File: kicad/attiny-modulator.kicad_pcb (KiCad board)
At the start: 2 copper layers, 0 parts

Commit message: Updating schematic, layout and front panel
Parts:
- added C1: 100nF, Rumblesan_Standard_Parts:C_Rect_L7.0mm_W2.5mm_P5.00mm, F.Cu at (153.2, 66.5)
- added C10: 100nF, Rumblesan_Standard_Parts:C_Rect_L7.0mm_W2.5mm_P5.00mm, F.Cu at (138.5, 110.0)
- added C12: 1nF, Rumblesan_Standard_Parts:C_Rect_L7.0mm_W2.5mm_P5.00mm, F.Cu at (145.8, 78.8)
- added C2: 100nF, Rumblesan_Standard_Parts:C_Rect_L7.0mm_W2.5mm_P5.00mm, F.Cu at (157.5, 63.0)
- added C3: 10uF, Rumblesan_Standard_Parts:CP_Radial_D5.0mm_P2.00mm, F.Cu at (144.3, 60.2)
- added C4: 1nF, Rumblesan_Standard_Parts:C_Rect_L7.0mm_W2.5mm_P5.00mm, F.Cu at (153.9, 100.3)
- added C5: 10uF, Rumblesan_Standard_Parts:CP_Radial_D5.0mm_P2.00mm, F.Cu at (150.9, 60.2)
- added C6: 100nF, Rumblesan_Standard_Parts:C_Rect_L7.0mm_W2.5mm_P5.00mm, F.Cu at (145.8, 89.4)
- added C7: 100nF, Rumblesan_Standard_Parts:C_Rect_L7.0mm_W2.5mm_P5.00mm, F.Cu at (156.7, 140.5)
- added C8: 100nF, Rumblesan_Standard_Parts:C_Rect_L7.0mm_W2.5mm_P5.00mm, F.Cu at (141.0, 137.8)
- added C9: 1n8F, Rumblesan_Standard_Parts:C_Rect_L7.0mm_W3.5mm_P5.00mm, F.Cu at (146.3, 125.0)
- added D1: 1N5158, Rumblesan_Standard_Parts:D_DO-41_SOD81_P10.16mm_Horizontal, F.Cu at (149.6, 55.6)
- added D2: 1N5158, Rumblesan_Standard_Parts:D_DO-41_SOD81_P10.16mm_Horizontal, F.Cu at (139.4, 52.3)
- added D3: LED, LED_THT:LED_D1.8mm_W3.3mm_H2.4mm, B.Cu at (115.8, 137.5)
- added D4: LED, LED_THT:LED_D1.8mm_W3.3mm_H2.4mm, B.Cu at (113.2, 141.0)
- added D5: LED, LED_THT:LED_D1.8mm_W3.3mm_H2.4mm, B.Cu at (105.2, 104.5)
- added D6: 1N4148, Rumblesan_Standard_Parts:D_DO-35_SOD27_P7.62mm_Horizontal, F.Cu at (116.0, 109.6)
- added H1: MountingHole_Pad, MountingHole:MountingHole_3.2mm_M3_DIN965_Pad, F.Cu at (103.5, 136.5)
- added H2: MountingHole_Pad, MountingHole:MountingHole_3.2mm_M3_DIN965_Pad, F.Cu at (103.5, 53.5)
- added H3: MountingHole_Pad, MountingHole:MountingHole_3.2mm_M3_DIN965_Pad, F.Cu at (134.5, 136.5)
- added H4: MountingHole_Pad, MountingHole:MountingHole_3.2mm_M3_DIN965_Pad, F.Cu at (134.5, 53.5)
- added J1: Eurorack Power Small, Eurorack_Power:Eurorack_PowerHeader_2x05_P2.54mm_Shrouded, F.Cu at (135.0, 64.5)
- added J10: Conn_01x04_Socket, Connector_PinSocket_2.54mm:PinSocket_1x04_P2.54mm_Vertical, F.Cu at (119.0, 71.0)
- added J11: Eurorack Mono Jack, Rumblesan_Standard_Parts:Jack_3.5mm_QingPu_WQP-PJ398SM_Vertical, B.Cu at (122.5, 149.5)
- added J12: Conn_01x05_Pin, Connector_PinHeader_2.54mm:PinHeader_1x05_P2.54mm_Vertical, B.Cu at (145.5, 145.5)
- added J13: Conn_01x05_Socket, Connector_PinSocket_2.54mm:PinSocket_1x05_P2.54mm_Vertical, F.Cu at (114.5, 145.5)
- added J2: Eurorack Mono Jack, Rumblesan_Standard_Parts:Jack_3.5mm_QingPu_WQP-PJ398SM_Vertical, B.Cu at (106.5, 123.5)
- added J3: Eurorack Mono Jack, Rumblesan_Standard_Parts:Jack_3.5mm_QingPu_WQP-PJ398SM_Vertical, B.Cu at (122.5, 104.5)
- added J4: Eurorack Mono Jack, Rumblesan_Standard_Parts:Jack_3.5mm_QingPu_WQP-PJ398SM_Vertical, B.Cu at (106.5, 149.5)
- added J5: Eurorack Mono Jack, Rumblesan_Standard_Parts:Jack_3.5mm_QingPu_WQP-PJ398SM_Vertical, B.Cu at (122.5, 123.5)
- added J6: AVR-ISP-6, Connector_PinHeader_2.54mm:PinHeader_2x03_P2.54mm_Vertical, F.Cu at (136.9, 116.3)
- added J7: Conn_01x04_Socket, Connector_PinSocket_2.54mm:PinSocket_1x04_P2.54mm_Vertical, F.Cu at (109.0, 83.0)
- added J8: Conn_01x04_Pin, Connector_PinHeader_2.54mm:PinHeader_1x04_P2.54mm_Vertical, B.Cu at (140.0, 83.0)
- added J9: Conn_01x04_Pin, Connector_PinHeader_2.54mm:PinHeader_1x04_P2.54mm_Vertical, B.Cu at (150.0, 71.0)
- added JP2: Jumper_2_Open, Connector_PinHeader_2.54mm:PinHeader_1x02_P2.54mm_Vertical, F.Cu at (153.2, 114.3)
- added JP3: Jumper_2_Open, Connector_PinHeader_2.54mm:PinHeader_1x02_P2.54mm_Vertical, F.Cu at (149.4, 116.8)
- added Q1: BC547, Package_TO_SOT_THT:TO-92_Inline_Wide, F.Cu at (102.6, 112.3)
- added Q2: BC547, Package_TO_SOT_THT:TO-92_Inline_Wide, F.Cu at (106.6, 95.0)
- added Q3: BC547, Package_TO_SOT_THT:TO-92_Inline_Wide, F.Cu at (111.5, 107.7)
- added R1: 200k, Rumblesan_Standard_Parts:R_Axial_DIN0207_L6.3mm_D2.5mm_P10.16mm_Horizontal, F.Cu at (151.9, 145.0)
- added R10: 100k, Rumblesan_Standard_Parts:R_Axial_DIN0207_L6.3mm_D2.5mm_P10.16mm_Horizontal, F.Cu at (150.9, 110.2)
- added R11: 100k, Rumblesan_Standard_Parts:R_Axial_DIN0207_L6.3mm_D2.5mm_P10.16mm_Horizontal, F.Cu at (142.7, 130.0)
- added R13: 10k, Rumblesan_Standard_Parts:R_Axial_DIN0207_L6.3mm_D2.5mm_P10.16mm_Horizontal, F.Cu at (152.9, 130.3)
- added R17: 1k, Rumblesan_Standard_Parts:R_Axial_DIN0207_L6.3mm_D2.5mm_P10.16mm_Horizontal, F.Cu at (126.5, 133.5)
- added R18: 100k, Rumblesan_Standard_Parts:R_Axial_DIN0207_L6.3mm_D2.5mm_P10.16mm_Horizontal, F.Cu at (116.3, 113.5)
- added R19: 10k, Rumblesan_Standard_Parts:R_Axial_DIN0207_L6.3mm_D2.5mm_P10.16mm_Horizontal, F.Cu at (113.5, 117.0)
- added R2: 200k, Rumblesan_Standard_Parts:R_Axial_DIN0207_L6.3mm_D2.5mm_P10.16mm_Horizontal, F.Cu at (136.4, 95.2)
- added R20: 100k, Rumblesan_Standard_Parts:R_Axial_DIN0207_L6.3mm_D2.5mm_P10.16mm_Horizontal, F.Cu at (102.0, 97.8)
- added R21: 47k, Rumblesan_Standard_Parts:R_Axial_DIN0207_L6.3mm_D2.5mm_P10.16mm_Horizontal, F.Cu at (105.4, 80.0)
- added R22: 100k, Rumblesan_Standard_Parts:R_Axial_DIN0207_L6.3mm_D2.5mm_P10.16mm_Horizontal, F.Cu at (111.5, 104.1)
- added R23: R_led, Rumblesan_Standard_Parts:R_Axial_DIN0207_L6.3mm_D2.5mm_P10.16mm_Horizontal, F.Cu at (102.4, 90.2)
- added R24: 200k, Rumblesan_Standard_Parts:R_Axial_DIN0207_L6.3mm_D2.5mm_P10.16mm_Horizontal, F.Cu at (158.0, 112.8)
- added R25: 200k, Rumblesan_Standard_Parts:R_Axial_DIN0207_L6.3mm_D2.5mm_P10.16mm_Horizontal, F.Cu at (154.9, 86.4)
- added R26: 100k, Rumblesan_Standard_Parts:R_Axial_DIN0207_L6.3mm_D2.5mm_P10.16mm_Horizontal, F.Cu at (151.9, 86.4)
- added R3: 200k, Rumblesan_Standard_Parts:R_Axial_DIN0207_L6.3mm_D2.5mm_P10.16mm_Horizontal, F.Cu at (148.8, 76.2)
- added R4: 200k, Rumblesan_Standard_Parts:R_Axial_DIN0207_L6.3mm_D2.5mm_P10.16mm_Horizontal, F.Cu at (158.0, 86.4)
- added R5: 100k, Rumblesan_Standard_Parts:R_Axial_DIN0207_L6.3mm_D2.5mm_P10.16mm_Horizontal, F.Cu at (157.0, 110.2)
- added R6: 1k, Rumblesan_Standard_Parts:R_Axial_DIN0207_L6.3mm_D2.5mm_P10.16mm_Horizontal, F.Cu at (141.0, 155.7)
- added R7: 100k, Rumblesan_Standard_Parts:R_Axial_DIN0207_L6.3mm_D2.5mm_P10.16mm_Horizontal, F.Cu at (147.8, 110.2)
- added R8: 100k, Rumblesan_Standard_Parts:R_Axial_DIN0207_L6.3mm_D2.5mm_P10.16mm_Horizontal, F.Cu at (139.7, 119.9)
- added R9: 100k, Rumblesan_Standard_Parts:R_Axial_DIN0207_L6.3mm_D2.5mm_P10.16mm_Horizontal, F.Cu at (149.9, 120.1)
- added RV1: 10k, Rumblesan_Standard_Parts:Potentiometer_Alpha_RD901F-40-00D_Single_Vertical, B.Cu at (122.5, 57.5)
- added RV2: 10k, Rumblesan_Standard_Parts:Potentiometer_Alpha_RD901F-40-00D_Single_Vertical, B.Cu at (106.5, 69.5)
- added RV3: 10k, Rumblesan_Standard_Parts:Potentiometer_Alpha_RD901F-40-00D_Single_Vertical, B.Cu at (122.5, 81.5)
- added U1: ATtiny85-20P, Package_DIP:DIP-8_W7.62mm, F.Cu at (144.3, 106.4)
- added U2: MCP602, Package_DIP:DIP-8_W7.62mm_Socket, F.Cu at (149.4, 97.0)
- added U4: L78L05_TO92, Package_TO_SOT_THT:TO-92_Inline_Wide, F.Cu at (145.0, 69.6)
- added U5: L79L05_TO92, Package_TO_SOT_THT:TO-92_Inline_Wide, F.Cu at (152.9, 53.8)
- added U6: TL072, Package_DIP:DIP-8_W7.62mm, F.Cu at (152.7, 132.8)
- added mouse-bite-2mm-slot: VAL**, Panelization:mouse-bite-2mm-slot, F.Cu at (130.0, 90.0)
- added mouse-bite-2mm-slot: VAL**, Panelization:mouse-bite-2mm-slot, F.Cu at (130.0, 110.0)
- added mouse-bite-2mm-slot: VAL**, Panelization:mouse-bite-2mm-slot, F.Cu at (130.0, 150.0)
- added mouse-bite-2mm-slot: VAL**, Panelization:mouse-bite-2mm-slot, F.Cu at (130.0, 130.0)
- added mouse-bite-2mm-slot: VAL**, Panelization:mouse-bite-2mm-slot, F.Cu at (130.0, 65.0)
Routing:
- net +5V: track 0.00 -> 146.7 mm
- net VCC: track 0.00 -> 112.1 mm
- net VEE: track 0.00 -> 103.0 mm
- net Net-(U2A--): track 0.00 -> 85.8 mm
- net -5V: track 0.00 -> 55.5 mm
- net /MCU_ADC_1: track 0.00 -> 52.3 mm
- net /OUT_MAIN: track 0.00 -> 52.1 mm
- net Net-(U2B--): track 0.00 -> 47.3 mm
- net /MCU_PWM: track 0.00 -> 39.3 mm
- net /CV2_MAIN: track 0.00 -> 38.0 mm
- net /CV1_CTRL: track 0.00 -> 32.4 mm
- net /MCU_ADC_2: track 0.00 -> 29.9 mm, vias 0 -> 1
- net Net-(J11-Tip): track 0.00 -> 29.4 mm
- net /CV2_CTRL: track 0.00 -> 28.0 mm
- net /POT1_CTRL: track 0.00 -> 26.7 mm
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- added copper zone on B.Cu, net GND
- added copper zone on F.Cu, net GND
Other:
- board outline added: 60 x 108 mm

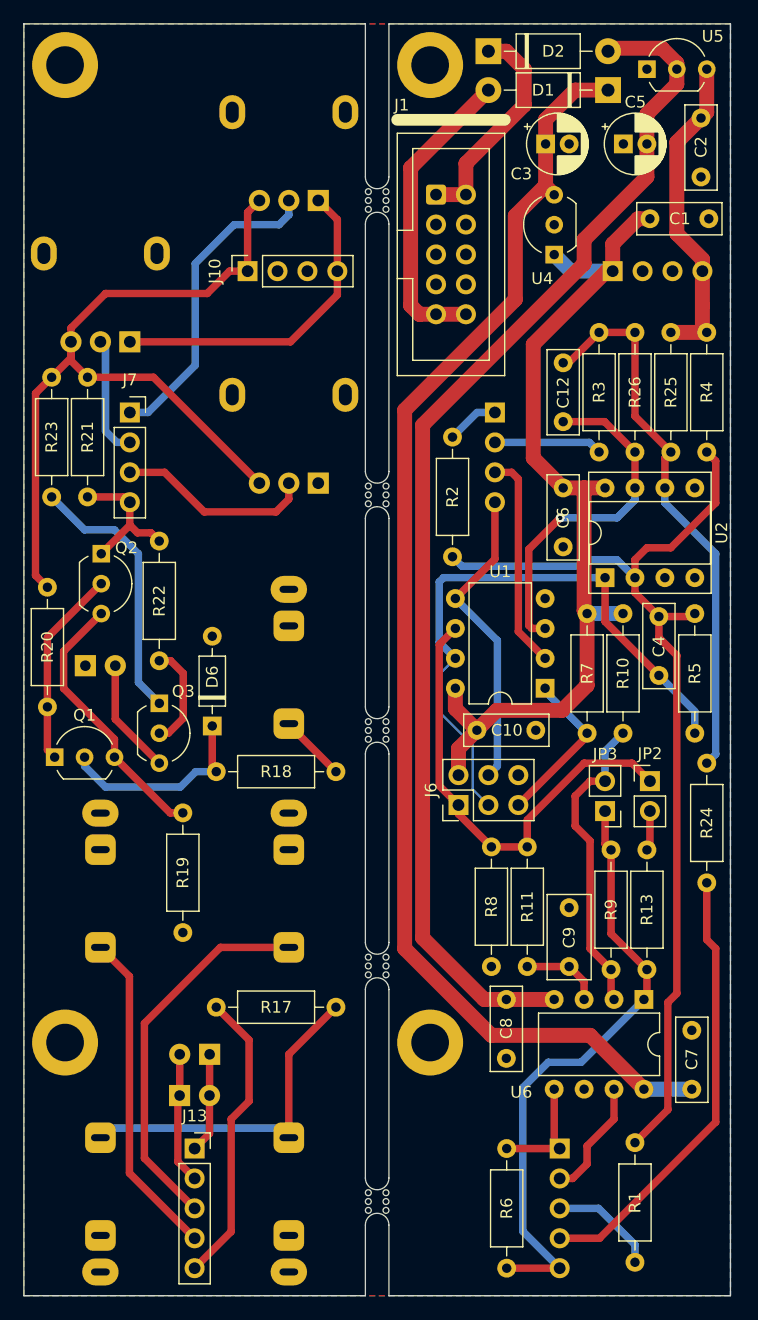
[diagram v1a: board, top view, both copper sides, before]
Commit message: Fixing bugs with circuit
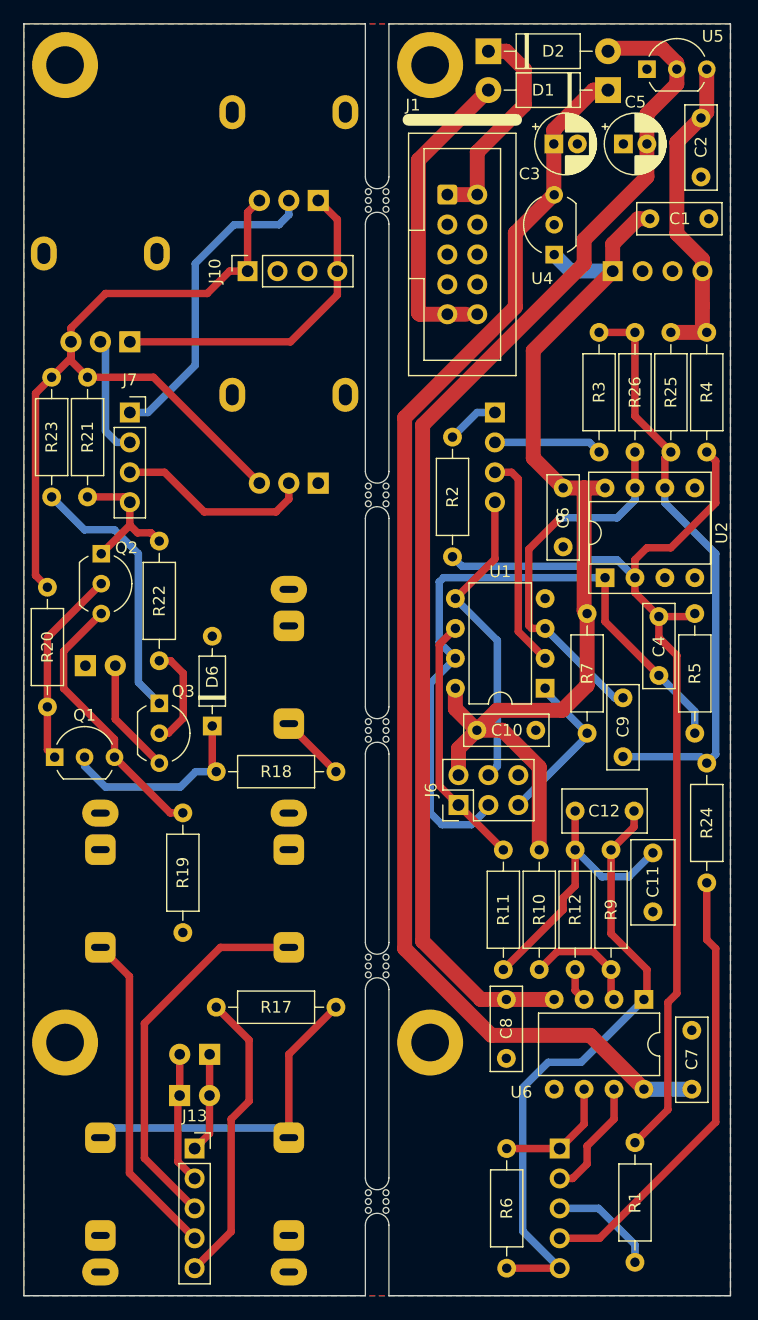
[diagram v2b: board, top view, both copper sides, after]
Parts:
- removed JP2, JP3: Jumper_2_Open, Connector_PinHeader_2.54mm:PinHeader_1x02_P2.54mm_Vertical
- removed R13: 10k, Rumblesan_Standard_Parts:R_Axial_DIN0207_L6.3mm_D2.5mm_P10.16mm_Horizontal
- removed R8: 100k, Rumblesan_Standard_Parts:R_Axial_DIN0207_L6.3mm_D2.5mm_P10.16mm_Horizontal
- added C11: 1nF, Rumblesan_Standard_Parts:C_Rect_L7.0mm_W3.5mm_P5.00mm, F.Cu at (153.4, 125.4)
- added R12: 22k, Rumblesan_Standard_Parts:R_Axial_DIN0207_L6.3mm_D2.5mm_P10.16mm_Horizontal, F.Cu at (146.8, 130.3)
- C12: value 1nF -> 2.2nF; footprint Rumblesan_Standard_Parts:C_Rect_L7.0mm_W2.5mm_P5.00mm -> Rumblesan_Standard_Parts:C_Rect_L7.0mm_W3.5mm_P5.00mm
- C9: value 1n8F -> 1nF; footprint Rumblesan_Standard_Parts:C_Rect_L7.0mm_W3.5mm_P5.00mm -> Rumblesan_Standard_Parts:C_Rect_L7.0mm_W2.5mm_P5.00mm
- R11: value 100k -> 22k
- moved C12 38.5 mm to (151.8, 116.8), turned to 180 degrees
- moved R10 21.3 mm to (143.8, 130.3)
- moved C9 13.6 mm to (150.9, 112.2), turned to 90 degrees
- moved R11 10.1 mm to (140.7, 120.1), turned to -90 degrees
- moved J1 0.96 mm to (136.0, 64.5)
- moved C3 0.70 mm to (145.0, 60.2)
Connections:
- C12 pad 1: Net-(U2B--) -> /OUT_MAIN
- C12 pad 2: /MCU_ADC_2 -> Net-(C11-Pad2)
- C9 pad 1: GND -> Net-(U2B--)
- C9 pad 2: Net-(U6A-+) -> /MCU_ADC_2
- J2 pad 3: unconnected-(J2-Tip_normalize-Pad3) -> GND
- J5 pad 3: unconnected-(J5-Tip_normalize-Pad3) -> GND
- R11 pad 1: Net-(U6A-+) -> /MCU_PWM
- R11 pad 2: /MCU_PWM -> Net-(C11-Pad2)
- U6 pad 5: /LED_NEG_MAIN -> GND
- U6 pad 6: GND -> /LED_NEG_MAIN
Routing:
- net Net-(C11-Pad2): track 0.00 -> 24.4 mm
- net /MCU_PWM: track 39.3 -> 21.6 mm
- net Net-(U6A--): track 26.4 -> 10.0 mm
- net +5V: track 146.7 -> 156.9 mm
- net /MCU_ADC_1: track 52.3 -> 57.8 mm
- net Net-(U6A-+): track 6.88 -> 2.86 mm
- net Net-(JP2-B): track 3.41 -> 0.00 mm
- net Net-(U2B--): track 47.3 -> 50.5 mm
- net VCC: track 112.1 -> 110.2 mm
- net /MCU_ADC_2: track 29.9 -> 31.8 mm
- net /LED_NEG_MAIN: track 9.73 -> 10.4 mm
- net /OUT_MAIN: track 52.1 -> 52.7 mm
- net Net-(D1-A): track 26.0 -> 25.5 mm

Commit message: Refreshing board layout
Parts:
- added REF**: BCM_Logo_tiny_Copper_8mmx8mm, BCM_Graphics:BCM_Logo_tiny_Copper_8mmx8mm, F.Cu at (135.4, 153.7)
- C11, C12: footprint Rumblesan_Standard_Parts:C_Rect_L7.0mm_W3.5mm_P5.00mm -> Rumblesan_Standard_Parts:C_Rect_L7.0mm_W2.5mm_P5.00mm
- J1: footprint Eurorack_Power:Eurorack_PowerHeader_2x05_P2.54mm_Shrouded -> Rumblesan_Eurorack_Power:Eurorack_PowerHeader_2x05_P2.54mm_Shrouded
- J11, J2, J3, J4, J5: footprint Rumblesan_Standard_Parts:Jack_3.5mm_QingPu_WQP-PJ398SM_Vertical -> Rumblesan_Audio_Connectors:Jack_3.5mm_QingPu_WQP-PJ398SM_Vertical
- RV1, RV2, RV3: footprint Rumblesan_Standard_Parts:Potentiometer_Alpha_RD901F-40-00D_Single_Vertical -> Rumblesan_Potentiometer_THT:Potentiometer_Alpha_RD901F-40-00D_Single_Vertical
- U1, U6: footprint Package_DIP:DIP-8_W7.62mm -> Package_DIP:DIP-8_W7.62mm_Socket
- mouse-bite-2mm-slot (x5): footprint Panelization:mouse-bite-2mm-slot -> Rumblesan_Panelization:mouse-bite-2mm-slot
- moved C7 0.25 mm to (156.7, 140.7)
- moved U6 0.25 mm to (152.7, 133.1)
- moved R6 0.22 mm to (141.2, 155.7)
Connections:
- R17 pad 1: Net-(J11-Tip) -> Net-(J11-PadT)
- R18 pad 2: Net-(J3-Tip) -> Net-(J3-PadT)
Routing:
- net Net-(J11-Tip): track 29.4 -> 0.00 mm
- net Net-(J11-PadT): track 0.00 -> 29.4 mm
- net Net-(J3-Tip): track 5.74 -> 0.00 mm
- net Net-(J3-PadT): track 0.00 -> 5.74 mm
- net /MCU_ADC_1: track 57.8 -> 53.6 mm
- net /MCU_ADC_2: track 31.8 -> 35.2 mm, vias 1 -> 0
- net +5V: track 156.9 -> 154.6 mm
- net /OUT_MAIN: track 52.7 -> 51.4 mm
- net /MCU_TRIG: track 26.4 -> 27.6 mm
- net /MCU_RESET: track 13.8 -> 15.0 mm
- net /LED_POS_MAIN: track 10.1 -> 9.24 mm
- net Net-(D2-K): track 18.5 -> 17.7 mm
- net VEE: track 103.2 -> 102.4 mm
- net Net-(U6A--): track 10.0 -> 10.7 mm
- net /MCU_PWM: track 21.6 -> 22.2 mm
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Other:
- outline, holes or cut-outs redrawn
- board text added: "Bristol Communal Modular ATTiny Modulator Rev 03"
- board text added: "THIS SIDE TO PANEL"
- board text added: "based on the JoyfulNoise Tiny Utility Board"
